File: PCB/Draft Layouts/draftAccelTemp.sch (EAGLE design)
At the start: 4 parts, among them U1 MMA8452Q

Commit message: Aileen's updates
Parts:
- removed ACCEL: 22-23-2041, con-molex:22-23-2041
- removed U1: MMA8452Q, SparkFun-Sensors:MMA8452Q
- added ACCEL1, ACCEL2, ACCEL3: 22-27-2041-04, con-molex:22-27-2041-04
- added C1: 1uF, rcl:C-USC0805
- added D1, D2, D3, D4: 1N4004, diode:1N4004
- added ECG: 22-27-2021-02, con-molex:22-27-2021-02
- added FRAM: 22-27-2081-08, con-molex:22-27-2081-08
- added IC3: AD623R, analog-devices:AD623R
- added R1, R2, R3: (no value), rcl:R-US_R0805
- added R4, R5: 330k, rcl:R-US_R0805
- added R6, R7: 560k, rcl:R-US_R0805
- TEMP: value 22-23-2041 -> 22-27-2081-08; device con-molex:22-23-2041 -> con-molex:22-27-2081-08
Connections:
- removed net N$3: TEMP-3.S
- new net A0: ACCEL3-4.S, TEMP-5.S
- new net A0FRAM: FRAM-1.S
- new net A1: TEMP-6.S
- new net A1FRAM: FRAM-2.S
- new net A2: TEMP-7.S
- new net A2FRAM: FRAM-3.S
- new net AGND: FRAM-4.S, FRAM-6.S, IC3.REF
- new net N$5: D1.A, D2.C, IC3.+, R4.2
- new net N$6: C1.1, IC3.OUT
- new net N$7: IC3.RG@2, R6.2
- new net N$8: IC3.RG@1, R6.1
- new net OS: R3.2, TEMP-4.S
- net GND: now also ACCEL1-4.S, ACCEL2-4.S, C1.2, D1.C, D2.A, D3.A, D4.C, IC3.-V, R7.1, R7.2, TEMP-8.S; no longer ACCEL-4.S, U1.GND
- net N$1: now also ECG-1.S, R4.1; no longer TEMP-1.S
- net N$2: now also D3.C, D4.A, IC3.-, R5.1; no longer TEMP-2.S
- net N$4: now also ECG-2.S, R5.2; no longer TEMP-4.S
- net SCL: now also ACCEL1-3.S, ACCEL2-3.S, FRAM-7.S, R2.2, TEMP-3.S; no longer ACCEL-3.S, U1.SCL
- net SDA: now also ACCEL1-2.S, ACCEL2-2.S, FRAM-8.S, R1.2, TEMP-2.S; no longer ACCEL-2.S, U1.SDA
- net VCC: now also ACCEL1-1.S, ACCEL2-1.S, FRAM-5.S, IC3.+V, R1.1, R2.1, R3.1, TEMP-1.S; no longer ACCEL-1.S, U1.VDD
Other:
- moved on the sheet: TEMP-1, TEMP-2, TEMP-3, TEMP-4

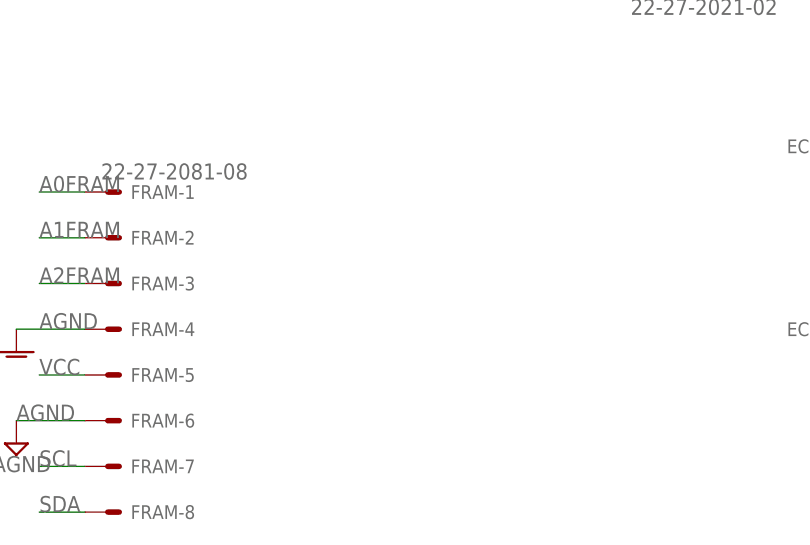
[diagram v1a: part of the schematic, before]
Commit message: new custom parts library
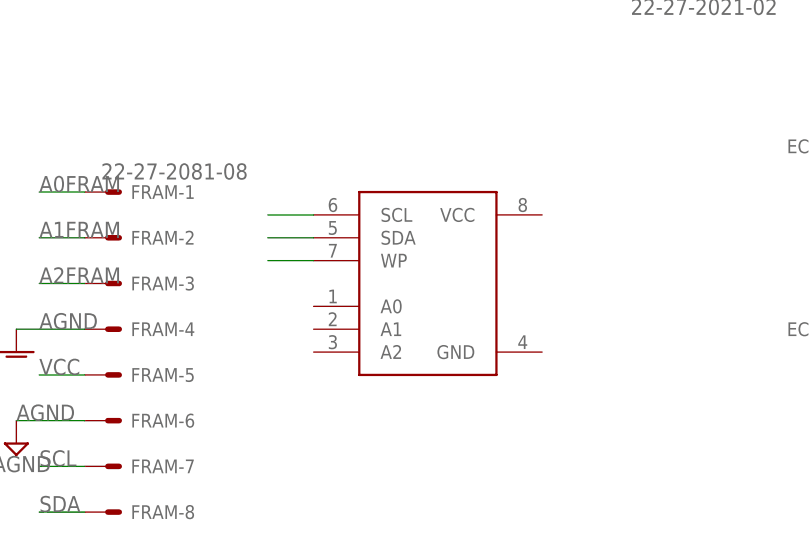
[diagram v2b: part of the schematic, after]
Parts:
- added U2: MB85RC256VPF-G-JNERE2, Custom Parts:MB85RC256VPF-G-JNERE2
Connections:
- new net N$10: U2.WP
- new net N$3: U2.SCL
- new net N$9: U2.SDA
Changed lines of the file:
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@@
 <?xml version="1.0" encoding="utf-8"?>
 <!DOCTYPE eagle SYSTEM "eagle.dtd">
-<eagle version="9.2.1">
+<eagle version="9.2.2">
 <drawing>
 <settings>
@@
 <layers>
 <layer number="1" name="Top" color="4" fill="1" visible="no" active="no"/>
+<layer number="2" name="Route2" color="16" fill="1" visible="no" active="no"/>
+<layer number="3" name="Route3" color="17" fill="1" visible="no" active="no"/>
+<layer number="4" name="Route4" color="18" fill="1" visible="no" active="no"/>
+<layer number="5" name="Route5" color="19" fill="1" visible="no" active="no"/>
+<layer number="6" name="Route6" color="25" fill="1" visible="no" active="no"/>
+<layer number="7" name="Route7" color="26" fill="1" visible="no" active="no"/>
+<layer number="8" name="Route8" color="27" fill="1" visible="no" active="no"/>
+<layer number="9" name="Route9" color="28" fill="1" visible="no" active="no"/>
+<layer number="10" name="Route10" color="29" fill="1" visible="no" active="no"/>
+<layer number="11" name="Route11" color="30" fill="1" visible="no" active="no"/>
+<layer number="12" name="Route12" color="20" fill="1" visible="no" active="no"/>
+<layer number="13" name="Route13" color="21" fill="1" visible="no" active="no"/>
+<layer number="14" name="Route14" color="22" fill="1" visible="no" active="no"/>
+<layer number="15" name="Route15" color="23" fill="1" visible="no" active="no"/>
 <layer number="16" name="Bottom" color="1" fill="1" visible="no" active="no"/>
 <layer number="17" name="Pads" color="2" fill="1" visible="no" active="no"/>
@@
 <part name="AGND2" library="supply1" library_urn="urn:adsk.eagle:library:371" deviceset="AGND" device=""/>
 <part name="SUPPLY7" library="supply2" library_urn="urn:adsk.eagle:library:372" deviceset="AGND" device=""/>
+<part name="U2" library="Custom Parts" deviceset="MB85RC256VPF-G-JNERE2" device=""/>
 </parts>
 <sheets>
@@
 <attribute name="VALUE" x="55.753" y="-20.955" size="1.778" layer="96"/>
 </instance>
+<instance part="U2" gate="G$1" x="96.52" y="-10.16" smashed="yes"/>
 </instances>
 <busses>
@@
 </segment>
 </net>
+<net name="N$3" class="0">
+<segment>
+<pinref part="U2" gate="G$1" pin="SCL"/>
+<wire x1="91.44" y1="7.62" x2="86.36" y2="7.62" width="0.1524" layer="91"/>
+</segment>
+</net>
+<net name="N$9" class="0">
+<segment>
+<pinref part="U2" gate="G$1" pin="SDA"/>
+<wire x1="91.44" y1="5.08" x2="86.36" y2="5.08" width="0.1524" layer="91"/>
+</segment>
+</net>
+<net name="N$10" class="0">
+<segment>
+<pinref part="U2" gate="G$1" pin="WP"/>
+<wire x1="91.44" y1="2.54" x2="86.36" y2="2.54" width="0.1524" layer="91"/>
+</segment>
+</net>
